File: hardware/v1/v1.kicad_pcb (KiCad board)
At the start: 2 copper layers, 139 x 99 mm, 77 parts, among them J1 AUDIO IN, J10 Close for battery power, J2 MIDI OUT, J3 MIDI IN, J4 MIDI THRU, J5 OUTPUT R, J6 OUTPUT L - MONO, J7 EXP 2, J8 EXP 1, J9 Batt In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

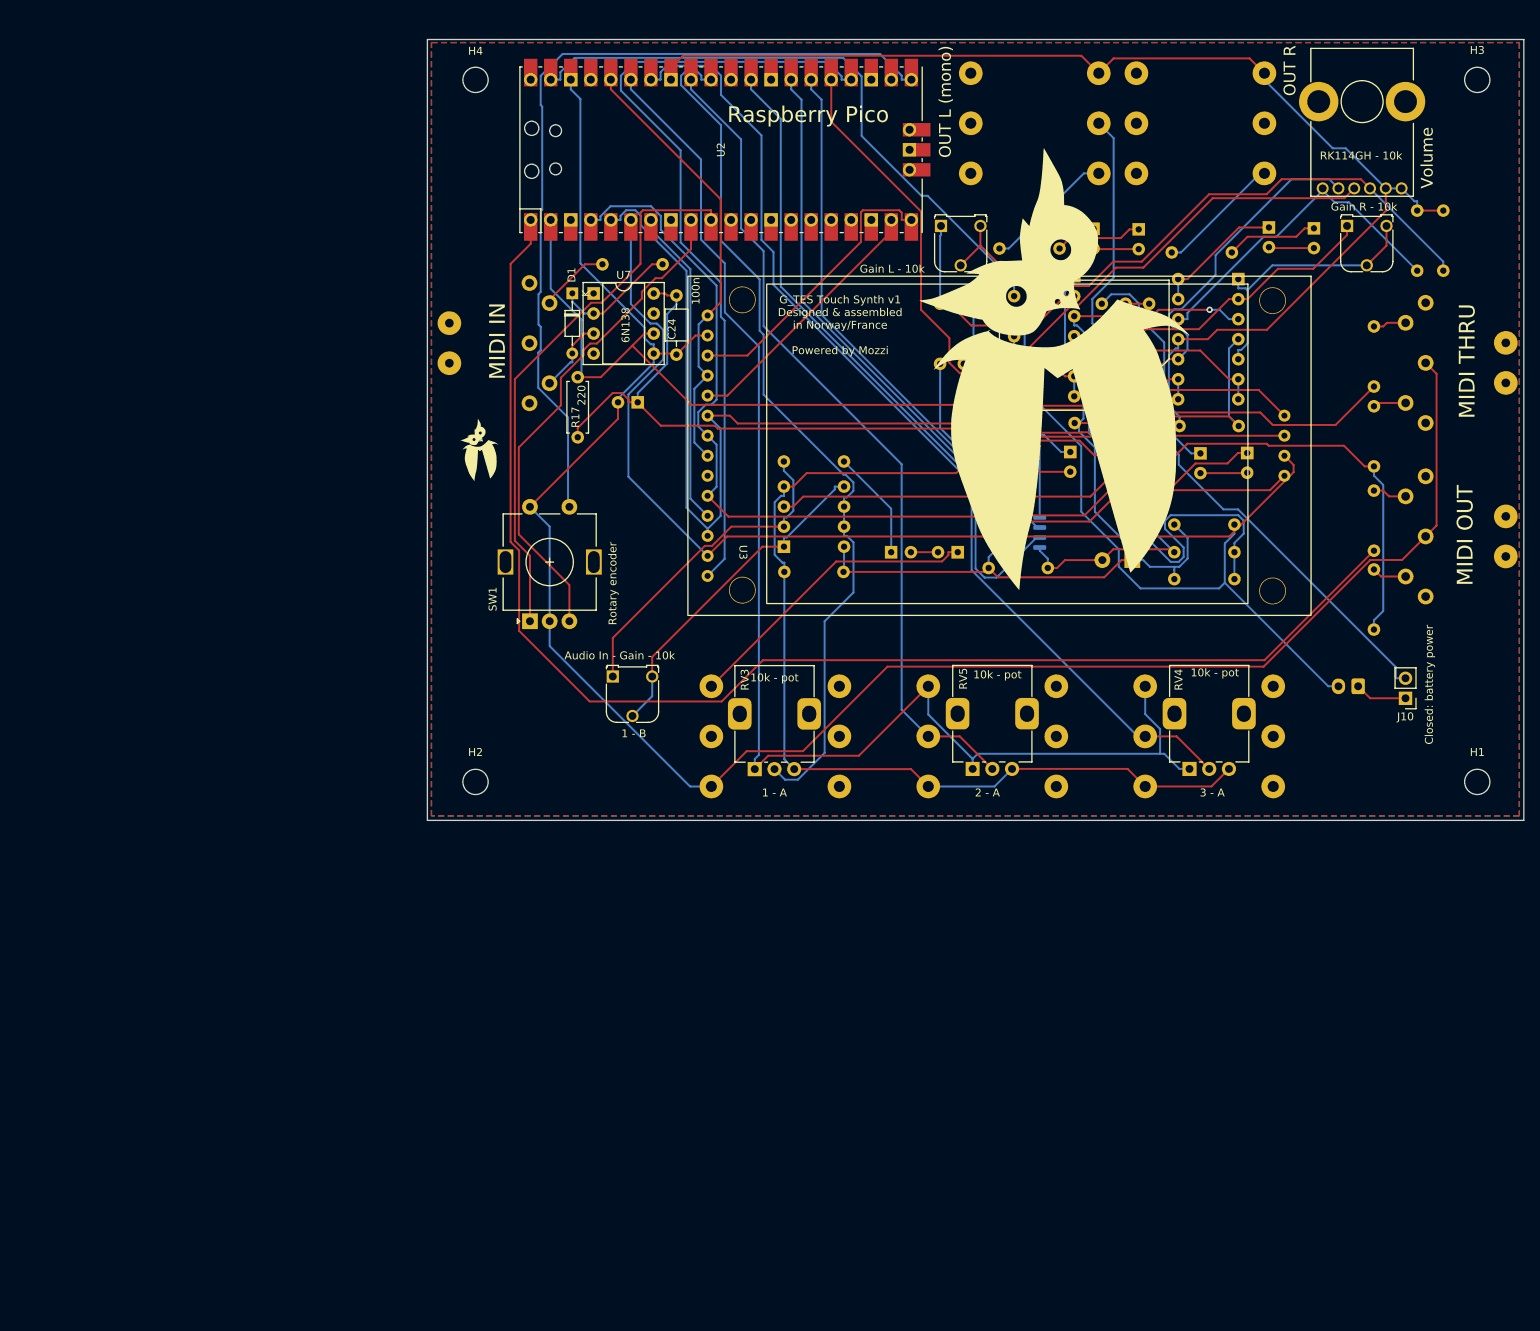
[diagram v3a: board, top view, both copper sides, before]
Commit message: Replace power selection with a switch
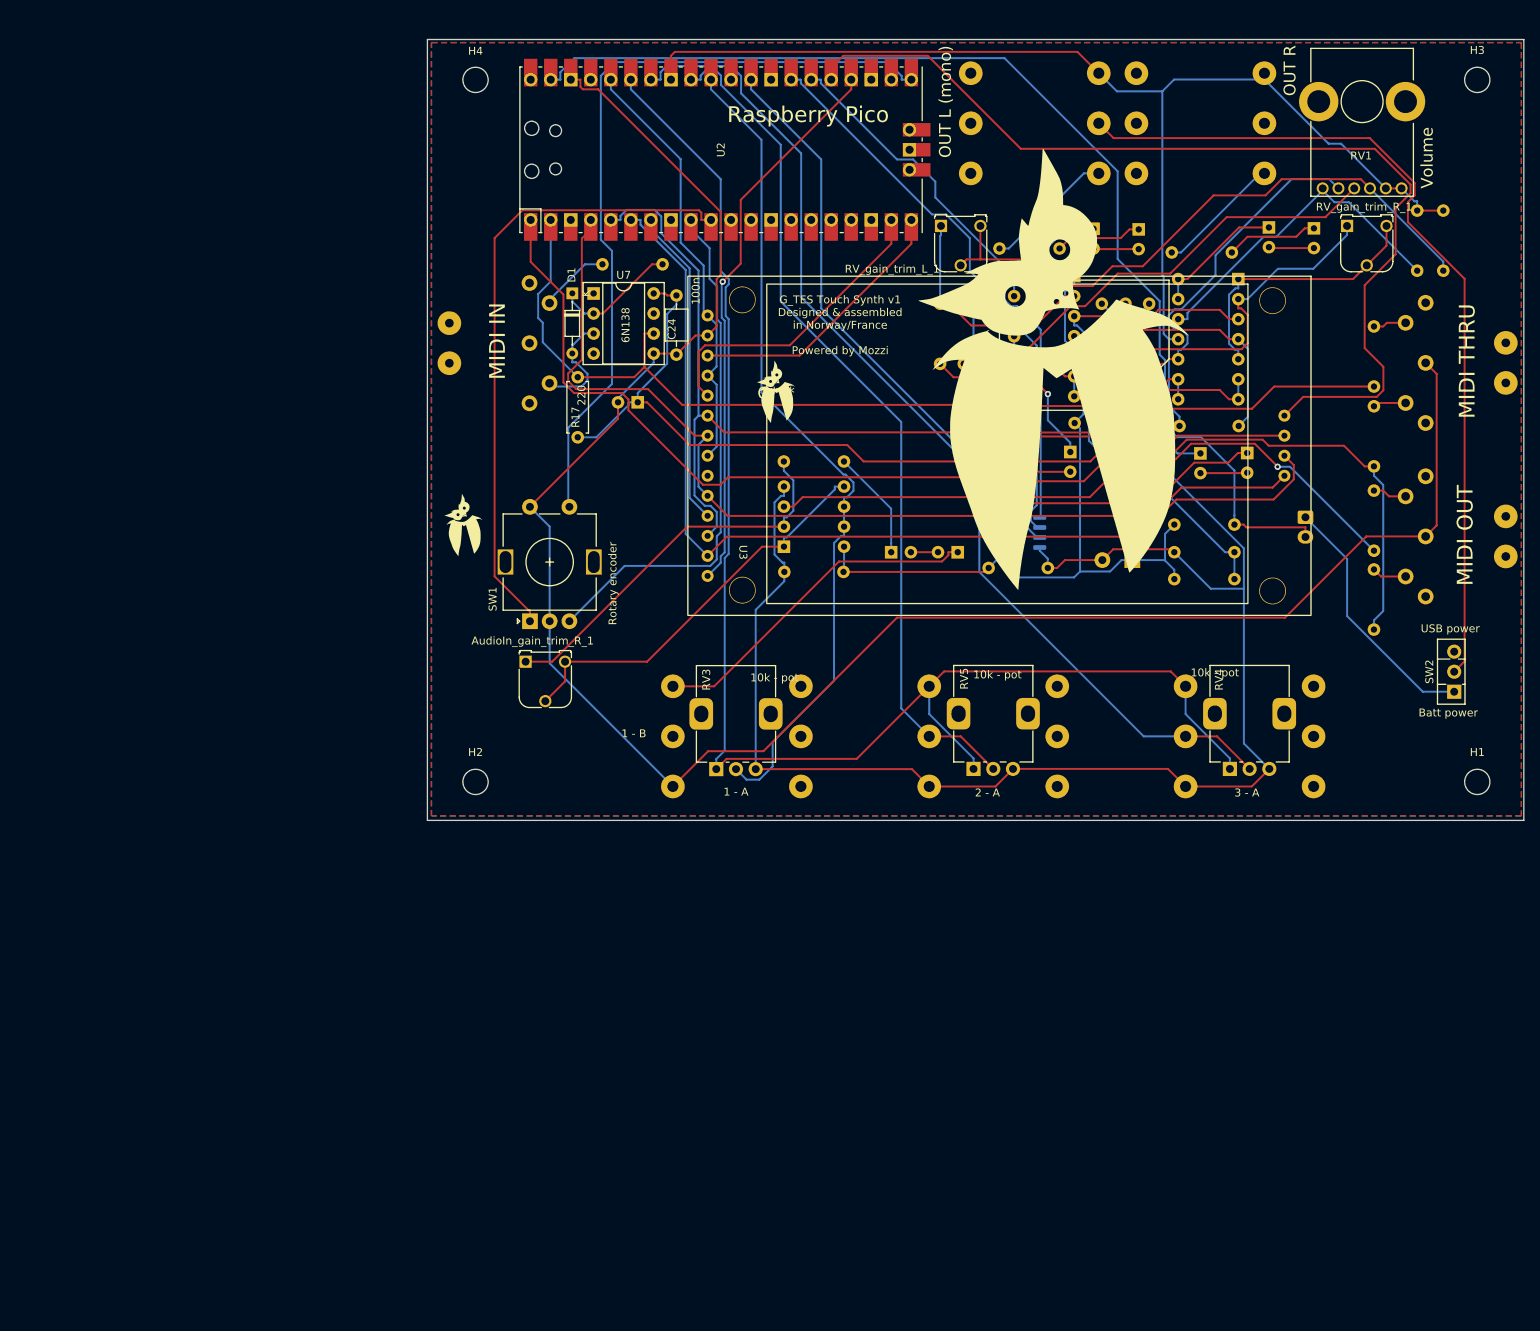
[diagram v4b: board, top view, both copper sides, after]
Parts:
- removed the G*** at (175.1, 83.6)
- removed the G*** at (102.1, 92.7)
- removed the G*** at (110.5, 118.1)
- removed J10: Close for battery power, Connector_PinHeader_2.54mm:PinHeader_1x02_P2.54mm_Vertical
- added G***: LOGO, PCB_symbols:owl_F_50x70, F.Cu at (175.0, 83.6)
- added G***: LOGO, PCB_symbols:owl_7x10, F.Cu at (100.1, 102.2)
- added G***: LOGO, PCB_symbols:owl_7x10, F.Cu at (139.7, 85.3)
- added G***: LOGO, PCB_symbols:owl_F_50x70, B.Cu at (110.9, 116.8)
- added SW2: SW_SPDT, Package_TO_SOT_THT:TO-126-3_Vertical, F.Cu at (225.7, 123.2)
- AudioIn_gain_trim_R_1: renamed from Audio In - Gain - 10k
- RV1: renamed from RK114GH - 10k
- RV_gain_trim_L_1: renamed from Gain L - 10k
- RV_gain_trim_R_1: renamed from Gain R - 10k
- moved J9 22.4 mm to (206.8, 101.1), turned to -90 degrees
- moved AudioIn_gain_trim_R_1 11.2 mm to (108.0, 119.4)
- moved J7 5.12 mm to (191.6, 122.5)
- moved RV4 5.12 mm to (197.2, 133.0)
- moved J1 4.88 mm to (126.6, 122.5)
- moved RV3 4.88 mm to (132.1, 133.0)
- moved J8 0.12 mm to (159.1, 122.5)
- moved RV5 0.12 mm to (164.7, 133.0)
- renumbered PT8211 to U1
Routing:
- net Net-(U2-Pad25): track 89.5 -> 125.7 mm
- net Net-(R16-Pad1): track 173.6 -> 139.5 mm, vias 0 -> 1
- net Net-(U2-Pad24): track 100.9 -> 70.8 mm, vias 0 -> 1
- net batt-: track 6.63 -> 32.3 mm
- net GNDA: track 358.1 -> 382.5 mm
- net batt+: track 161.3 -> 142.6 mm
- net virtual_mass: track 128.2 -> 110.4 mm, vias 1 -> 0
- net ADC_VREF: track 171.4 -> 184.5 mm
- net Net-(J6-PadR): track 96.4 -> 109.0 mm
- net Net-(U2-Pad5): track 140.5 -> 129.3 mm
- net Net-(SW1-PadA): track 70.2 -> 80.5 mm
- net Net-(AudioIn_gain_trim_R_1-Pad2): track 42.7 -> 51.5 mm
- net Net-(SW1-PadS1): track 106.6 -> 98.9 mm
- net Net-(AudioIn_gain_trim_R_1-Pad1): track 41.9 -> 49.3 mm
- net Net-(J7-PadR): track 127.1 -> 133.2 mm
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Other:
- board text added: "Batt power"
- board text added: "USB power"
- board text removed: "Closed: battery power"

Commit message: Added dial serigraphy
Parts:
- added G***: LOGO, pot_dials:pot_dial, F.Cu at (167.3, 125.0)
- added G***: LOGO, pot_dials:pot_dial, F.Cu at (134.7, 124.9)
- added G***: LOGO, pot_dials:rot_dial, F.Cu at (110.8, 106.7)
- added G***: LOGO, pot_dials:pot_dial, F.Cu at (199.7, 125.1)
- added G***: LOGO, pot_dials:pot_dial, F.Cu at (214.1, 48.1)
- moved G*** 9.20 mm to (100.8, 93.1)
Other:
- board text added: "T E S"

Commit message: Better ground plane?
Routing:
- net Net-(U1-Pad1): track 70.0 -> 75.8 mm
- net Net-(U1-Pad2): track 72.8 -> 77.0 mm
- net Net-(R17-Pad1): track 133.1 -> 134.5 mm

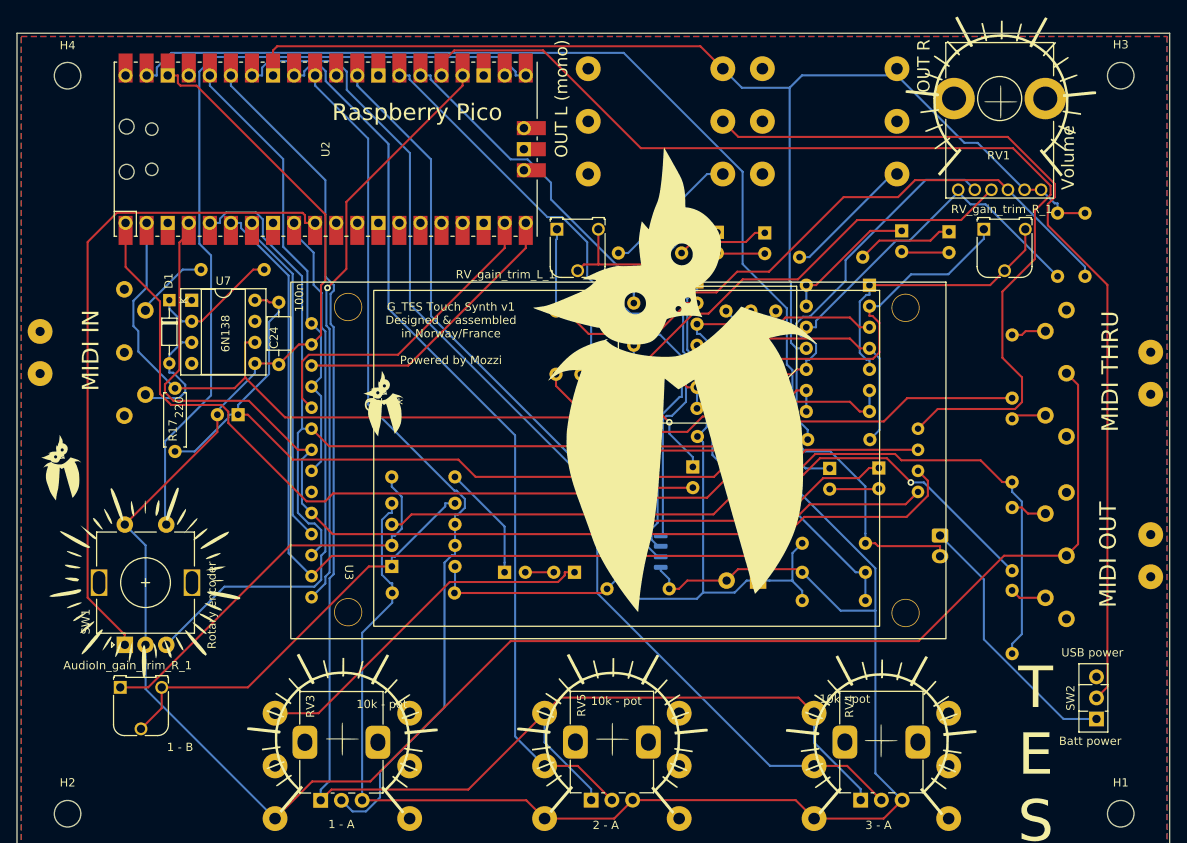
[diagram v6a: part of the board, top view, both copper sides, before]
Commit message: Improved silk
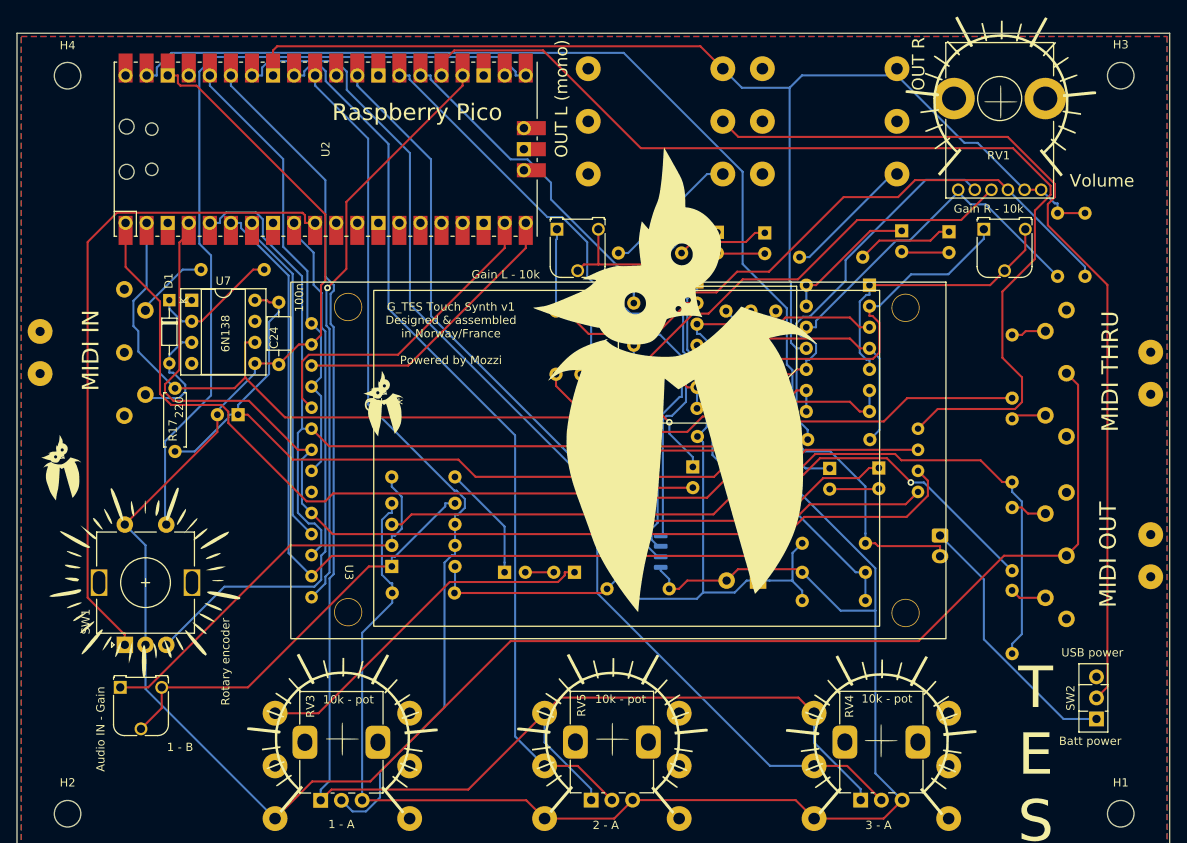
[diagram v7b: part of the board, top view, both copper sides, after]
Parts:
- Gain L - 10k: renamed from RV_gain_trim_L_1
- Gain R - 10k: renamed from RV_gain_trim_R_1
- renumbered J9 to Batt
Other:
- board text added: "100"
- board text added: "Audio IN - Gain"
- board text added: "PT8211"
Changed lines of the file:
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@@
     (property "Sheetname" "")
     (attr through_hole)
-    (fp_text reference "RV_gain_trim_R_1" (at 2.159 -2.413) (layer "F.SilkS")
+    (fp_text reference "Gain R - 10k" (at 0.5842 -2.4638) (layer "F.SilkS")
       (effects (font (size 1 1) (thickness 0.15)))
     )
@@
     (property "Sheetname" "")
     (attr through_hole)
-    (fp_text reference "RV_gain_trim_L_1" (at -6.176 5.461) (layer "F.SilkS")
+    (fp_text reference "Gain L - 10k" (at -6.176 5.461) (layer "F.SilkS")
       (effects (font (size 1 1) (thickness 0.15)))
     )
@@
     (property "Sheetname" "")
     (attr through_hole)
-    (fp_text reference "AudioIn_gain_trim_R_1" (at 0.888 -2.642) (layer "F.SilkS")
+    (fp_text reference "AudioIn_gain_trim_R_1" (at 0.888 -2.642) (layer "F.SilkS") hide
       (effects (font (size 1 1) (thickness 0.15)))
     )
@@
     (property "Sheetname" "")
     (attr through_hole)
-    (fp_text reference "J9" (at 1.25 3.55 90) (layer "B.SilkS")
+    (fp_text reference "Batt" (at 1.25 3.55 90) (layer "B.SilkS")
       (effects (font (size 1 1) (thickness 0.15)) (justify mirror))
     )
@@
     (property "Sheetname" "")
     (attr through_hole)
-    (fp_text reference "R12" (at 3.81 2.37) (layer "B.SilkS")
+    (fp_text reference "R12" (at 5.1816 -0.4958) (layer "B.SilkS")
       (effects (font (size 1 1) (thickness 0.15)) (justify mirror))
     )
@@
     (property "Sheetname" "")
     (attr through_hole)
-    (fp_text reference "R13" (at 3.81 2.37) (layer "B.SilkS")
+    (fp_text reference "R13" (at 5.2832 -0.4878) (layer "B.SilkS")
       (effects (font (size 1 1) (thickness 0.15)) (justify mirror))
     )
@@
     (effects (font (size 1 1) (thickness 0.15)) (justify mirror))
   )
+  (gr_text "100" (at 195.5038 67.056) (layer "B.SilkS")
+    (effects (font (size 1 1) (thickness 0.15)) (justify mirror))
+  )
   (gr_text "10k" (at 163.068 78.994 90) (layer "B.SilkS")
     (effects (font (size 1 1) (thickness 0.15)) (justify mirror))
@@
     (effects (font (size 1 1) (thickness 0.15)) (justify mirror))
   )
+  (gr_text "100" (at 173.2534 66.548) (layer "B.SilkS")
+    (effects (font (size 1 1) (thickness 0.15)) (justify mirror))
+  )
   (gr_text "10u" (at 201.93 69.215) (layer "B.SilkS")
     (effects (font (size 1 1) (thickness 0.15)) (justify mirror))
   )
+  (gr_text "10u" (at 180.6702 69.1642) (layer "B.SilkS")
+    (effects (font (size 1 1) (thickness 0.15)) (justify mirror))
+  )
   (gr_text "10u" (at 161.417 109.093) (layer "B.SilkS")
     (effects (font (size 1 1) (thickness 0.15)) (justify mirror))
   )
+  (gr_text "PT8211" (at 175.4124 102.6922 90) (layer "B.SilkS")
+    (effects (font (size 1 1) (thickness 0.15)) (justify mirror))
+  )
   (gr_text "33" (at 215.138 113.284 90) (layer "B.SilkS")
     (effects (font (size 1 1) (thickness 0.15)) (justify mirror))
   )
+  (gr_text "10u" (at 186.5122 69.2912) (layer "B.SilkS")
+    (effects (font (size 1 1) (thickness 0.15)) (justify mirror))
+  )
   (gr_text "1k" (at 224.028 67.437 90) (layer "B.SilkS")
     (effects (font (size 1 1) (thickness 0.15)) (justify mirror))
@@
     (effects (font (size 1 1) (thickness 0.15)))
   )
-  (gr_text "Volume\n" (at 222.25 55.499 90) (layer "F.SilkS")
+  (gr_text "Volume\n" (at 226.3394 58.293) (layer "F.SilkS")
     (effects (font (size 1.5 1.5) (thickness 0.2)))
   )
-  (gr_text "OUT R" (at 204.851 44.45 90) (layer "F.SilkS")
+  (gr_text "OUT R" (at 204.216 44.196 90) (layer "F.SilkS")
     (effects (font (size 1.5 1.5) (thickness 0.25)))
   )
@@
     (effects (font (size 2 2) (thickness 0.5)))
   )
-  (gr_text "10k - pot" (at 195.326 120.777) (layer "F.SilkS")
+  (gr_text "10k - pot" (at 200.406 120.7516) (layer "F.SilkS")
     (effects (font (size 1 1) (thickness 0.15)))
   )
@@
     (effects (font (size 5 5) (thickness 1.25)))
   )
-  (gr_text "Rotary encoder" (at 118.999 109.474 90) (layer "F.SilkS")
+  (gr_text "Rotary encoder" (at 120.65 116.2812 90) (layer "F.SilkS")
     (effects (font (size 1 1) (thickness 0.15)))
   )
@@
     (effects (font (size 2 2) (thickness 0.5)))
   )
+  (gr_text "Audio IN - Gain" (at 105.5878 124.4092 90) (layer "F.SilkS")
+    (effects (font (size 1 1) (thickness 0.15)))
+  )
   (gr_text "100n" (at 129.54 72.39 90) (layer "F.SilkS")
     (effects (font (size 1 1) (thickness 0.15)))
@@
     (effects (font (size 1 1) (thickness 0.15)))
   )
-  (gr_text "10k - pot" (at 139.4995 121.412) (layer "F.SilkS")
+  (gr_text "10k - pot" (at 135.4582 120.8532) (layer "F.SilkS")
     (effects (font (size 1 1) (thickness 0.15)))
   )
-  (gr_text "10k - pot" (at 167.767 121.031) (layer "F.SilkS")
+  (gr_text "10k - pot" (at 168.275 120.8024) (layer "F.SilkS")
     (effects (font (size 1 1) (thickness 0.15)))
   )

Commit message: Updated pcb
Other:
- board text removed: "Batteries (4xAA)"
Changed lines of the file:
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@@
     (at 139.7 85.344)
     (attr board_only exclude_from_pos_files exclude_from_bom)
-    (fp_text reference "G***" (at 0 0) (layer "F.SilkS")
+    (fp_text reference "G***" (at 0 0) (layer "F.SilkS") hide
       (effects (font (size 1.524 1.524) (thickness 0.3)))
     )
@@
   (gr_line (start 182.626 90.932) (end 182.626 90.551) (layer "B.SilkS") (width 0.15))
   (gr_line (start 151 109) (end 151 109.5) (layer "B.SilkS") (width 0.15))
-  (gr_rect (start 374 230) (end 432 293) (layer "Dwgs.User") (width 0.15) (fill none))
   (gr_rect (start 234.5 139.5) (end 95.5 40.5) (layer "Edge.Cuts") (width 0.1) (fill none))
   (gr_text "100u" (at 120.904 91.44) (layer "B.SilkS")
@@
     (effects (font (size 1 1) (thickness 0.15)) (justify mirror))
   )
-  (gr_text "100" (at 195.5038 67.056) (layer "B.SilkS")
+  (gr_text "100" (at 195.326 67.056) (layer "B.SilkS")
     (effects (font (size 1 1) (thickness 0.15)) (justify mirror))
   )
@@
     (effects (font (size 1.5 1.5) (thickness 0.2)))
   )
-  (gr_text "OUT R" (at 204.216 44.196 90) (layer "F.SilkS")
+  (gr_text "OUT R" (at 204.47 43.9166 90) (layer "F.SilkS")
     (effects (font (size 1.5 1.5) (thickness 0.25)))
   )
@@
     (effects (font (size 1 1) (thickness 0.15)))
   )
-  (gr_text "Batteries (4xAA)\n" (at 403 236) (layer "Dwgs.User")
-    (effects (font (size 1 1) (thickness 0.15)))
-  )
   (segment (start 140.7 102.26) (end 128.4361 102.26) (width 0.25) (layer "F.Cu") (net 1))
   (segment (start 111.3161 119.38) (end 107.95 119.38) (width 0.25) (layer "F.Cu") (net 1))
@@
     )
   )
-  (group "" (id b3834edf-6708-459c-8bc8-432465abe826)
-    (members
-      508a9e2a-a79e-49ef-bf95-d83def610f68
-      7eee0136-7150-4a55-9e9b-f446b1d1902b
-    )
-  )
